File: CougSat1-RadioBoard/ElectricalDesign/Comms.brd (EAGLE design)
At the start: 91.4 x 95.8 mm, 427 parts, among them J1 230mm Antenna, J2 CougSat Card, J3 230mm Antenna, J4 SWD, Q1 CSD25402Q3A, Q10 DMN53D0LDW, Q11 MMBTA06W, Q12 MMBTA06W, Q13 DMN53D0LDW, Q14 DMP2065UFDB, Q15 MMBTA06W, Q16 CSD25402Q3A, Q17 CSD25402Q3A, Q2 CSD25402Q3A, Q3 CSD25402Q3A, Q4 DMN53D0LDW, Q5 DMN53D0LDW, Q6 CSD25402Q3A, Q7 CSD25402Q3A, Q8 CSD25402Q3A, Q9 DMN53D0LDW, U1 TPS73250, U10 MAAP-011232, U11 LTC2499, U12 LTC2499, U13 LTC2499, U14 LP5907MFX-3.1, U15 TPS73250, U16 AD8137, U17 STM32L496RGT, U18 AD8137, U19 MAAP-011232, U2 LP5907MFX-3.1, U20 ADF4360, U21 HMC545A, U22 AD8515, U23 MAAM-011229, U24 AD8515, U25 MAAM-011229, U26 AD8345, U27 LM2776, U28 AS8348, U29 MCP1501-18, U3 TPS61236, U30 TXS0102DQM, U31 MAAM-011229, U32 AD8515, U33 AD8515, U34 AD8515, U35 TXS0102DQM, U36 ADF4360, U37 AD8515, U38 AD8515, U39 AD8515, U4 AD8346, U40 AD8515, U41 AD8137, U42 AD8137, U43 LP5907MFX-3.1, U44 TPS73250, U5 ADF4360, U6 TPS61089, U7 MAAM-011229, U8 IS25LP016D, U9 IS25LP016D, Y1 20MHz ±2.5ppm, Y2 32.768kHz ±10ppm, Y3 16MHz ±10ppm, Y4 20MHz ±2.5ppm, Y5 20MHz ±2.5ppm

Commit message: Created mCAD
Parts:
- removed LOGO3: SIGNATUREBRADLEY, CougsInSpace-Aesthetics:SIGN-BRADLEY
- added LOGO201: Speed Limit, CougsInSpace-Aesthetics:SPEED_LIMIT
- LOGO1: value Speed Limit -> SIGNATUREBRADLEY; device CougsInSpace-Aesthetics:SPEED_LIMIT -> CougsInSpace-Aesthetics:SIGN-BRADLEY
- moved LOGO1 55.1 mm to (8.30, -2.70), flipped to the top
- renumbered C133 to C200, C134 to C201, C135 to C202, C136 to C203, C137 to C204, C138 to C205, C139 to C206, C140 to C207, C141 to C208, C142 to C209, C143 to C210, C144 to C211, C145 to C212, C146 to C213, C147 to C214, C148 to C215, C149 to C216, C150 to C217, C151 to C218, C152 to C219, C153 to C220, C154 to C221, C155 to C222, C156 to C223, C157 to C224, C158 to C225, C159 to C226, C160 to C227, C161 to C228, C162 to C229, C163 to C230, J4 to J200, LOGO2 to LOGO200, R125 to R200, R126 to R201, R127 to R202, R128 to R203, R129 to R204, R130 to R205, R131 to R206, RT10 to RT205, RT11 to RT206, RT12 to RT207, RT13 to RT208, RT14 to RT209, RT15 to RT210, RT16 to RT211, RT17 to RT212, RT18 to RT213, RT19 to RT214, RT20 to RT215, RT21 to RT216, RT22 to RT217, RT5 to RT200, RT6 to RT201, RT7 to RT202, RT8 to RT203, RT9 to RT204, TP1 to TP200, TP2 to TP201, TP3 to TP202, TP4 to TP203, TP5 to TP204, Z2 to Z1

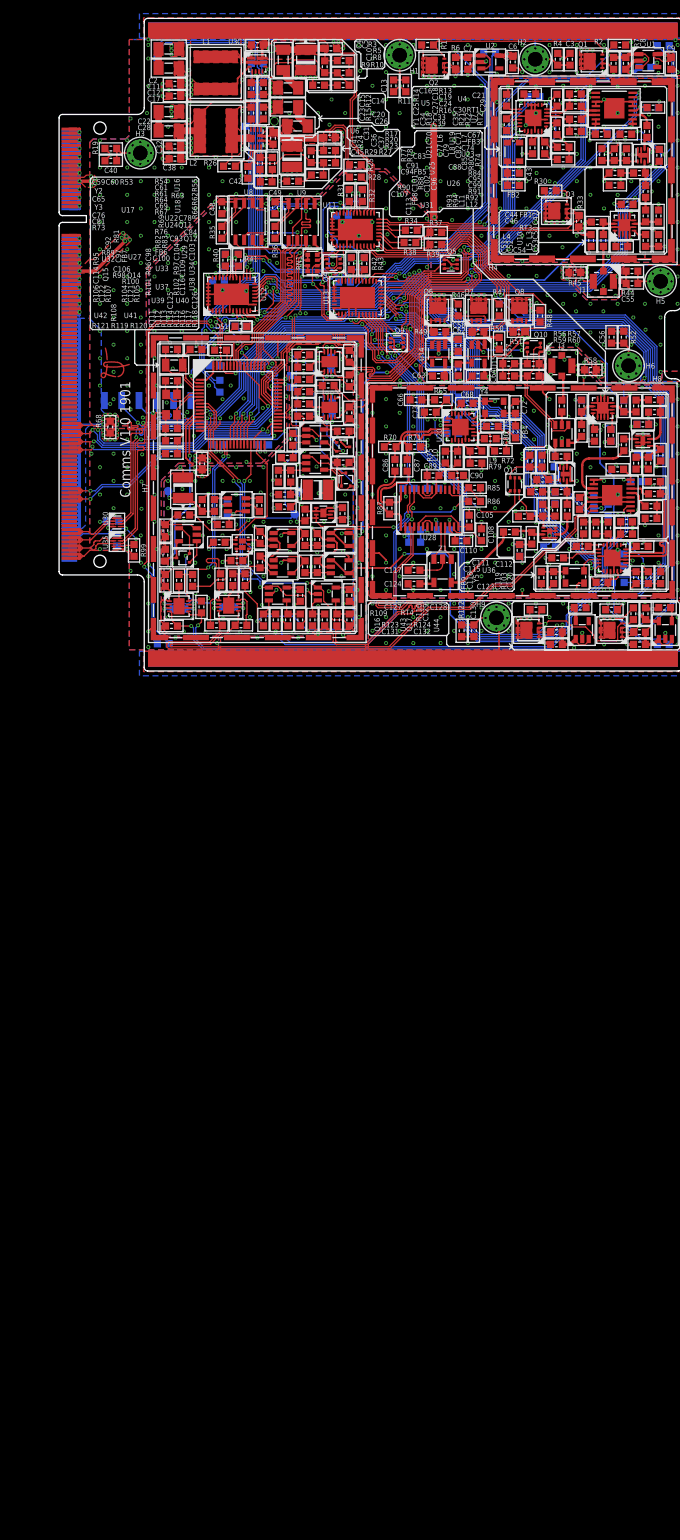
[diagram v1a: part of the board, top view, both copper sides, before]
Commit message: Edited ADCs and RF Clock Generators
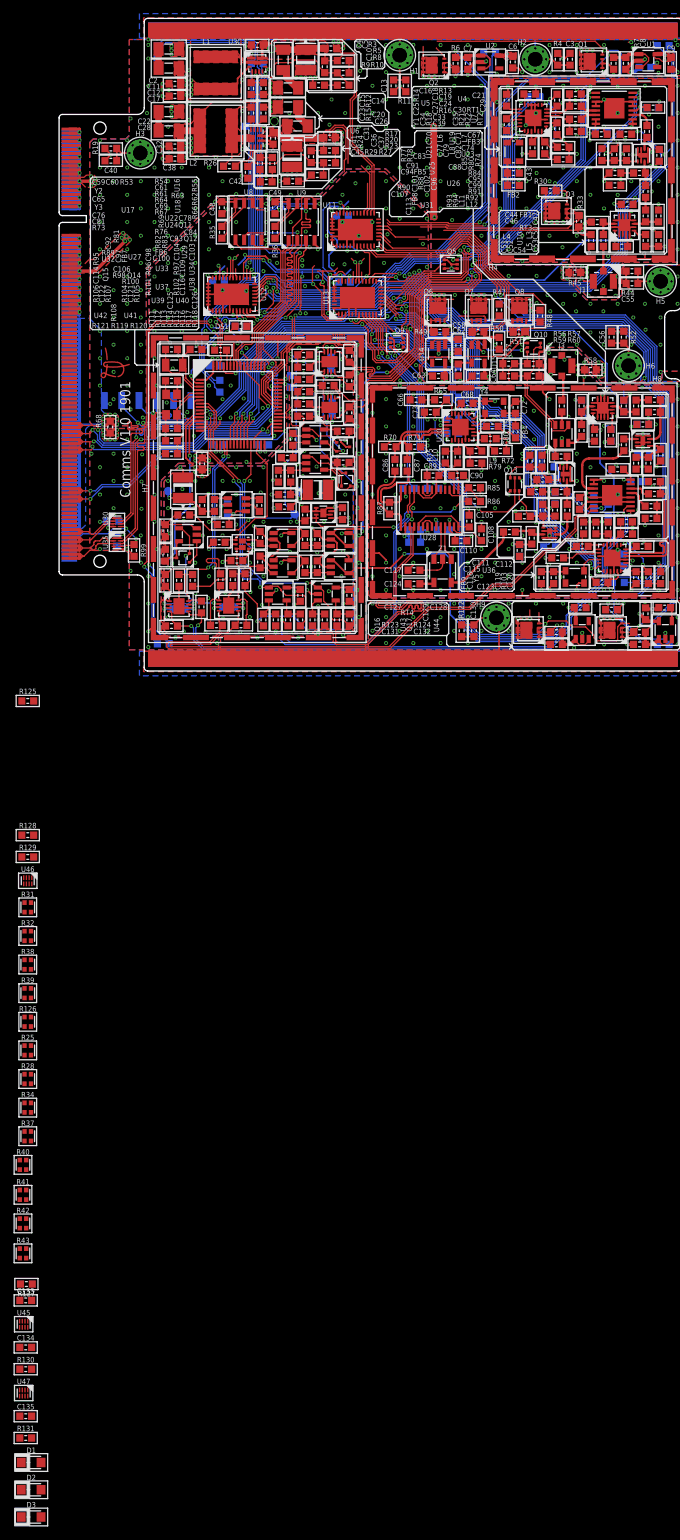
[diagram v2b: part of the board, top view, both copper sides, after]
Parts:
- removed Q4: DMN53D0LDW, CougsInSpace-DiscreteSemi:SOT363
- removed R1, R109, R110, R2, R46: 10kΩ 0.1%, CougsInSpace-Resistors:1608
- removed R201, R202, R203, R204, R205, R206: 8.45kΩ 0.1%, CougsInSpace-Resistors:1608
- removed RN1: 10kΩ 1%, CougsInSpace-Resistors:1632
- added C133, C134, C135: 100nF 10%, CougsInSpace-Capacitors:1608
- added D1, D2, D3: SS1FH10, CougsInSpace-DiscreteSemi:DO-219AB
- added R125: 1kΩ 0.1%, CougsInSpace-Resistors:1608
- added R126: 20kΩ 0.1%, CougsInSpace-Resistors:1616
- added R127, R128, R129, R130, R131: 10kΩ 0.1%, CougsInSpace-Resistors:1608
- added U45, U46, U47: TXS0102DQM, CougsInSpace-IC-Comms:X2SON-8
- R25, R37, R39: value 47kΩ 0.1% -> 50kΩ 0.1%; device CougsInSpace-Resistors:1608 -> CougsInSpace-Resistors:1616
- R28, R34, R38: value 47kΩ 0.1% -> 20kΩ 0.1%; device CougsInSpace-Resistors:1608 -> CougsInSpace-Resistors:1616
- R31, R40, R42: value 39.2kΩ 0.1% -> 20kΩ 0.1%; device CougsInSpace-Resistors:1608 -> CougsInSpace-Resistors:1616
- R32, R41, R43: value 39.2kΩ 0.1% -> 5kΩ 0.1%; device CougsInSpace-Resistors:1608 -> CougsInSpace-Resistors:1616
- moved R43 153.7 mm to (-5.30, -133.4), turned to 0 degrees
- moved R42 148.9 mm to (-5.30, -129.0), turned to 0 degrees
- moved R37 145.6 mm to (-4.60, -116.2), turned to 0 degrees
- moved R28 140.9 mm to (-4.60, -107.8)
- moved R41 140.8 mm to (-5.30, -124.8), turned to 0 degrees
- moved R34 140.6 mm to (-4.60, -112.0), turned to 0 degrees
- moved R25 138.6 mm to (-4.60, -103.6)
- moved R40 136.1 mm to (-5.30, -120.4), turned to 0 degrees
- moved R39 125.2 mm to (-4.60, -95.2), turned to 0 degrees
- moved R38 119.9 mm to (-4.60, -91.0), turned to 0 degrees
- moved R32 119.3 mm to (-4.60, -86.8), turned to 0 degrees
- moved R31 114.7 mm to (-4.60, -82.6), turned to 0 degrees
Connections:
- removed net I2C_SCL_5V: Q4.6, RN1.4, U11.2
- removed net I2C_SDA_5V: Q4.3, RN1.3, U11.3
- new net ADC_5.0V: R28.2, U11.20
- new net ADC_5.0V_I: R28.1, U11.21
- new net ADC_I_5.0V-0N: R34.1, U11.19
- new net ADC_I_5.0V-0P: R34.2, U11.18
- new net ADC_I_5.0V-1N: R126.4, U11.11
- new net ADC_I_5.0V-1P: R126.3, U11.10
- new net ADC_I_5.0V-2N: R38.4, U11.13
- new net ADC_I_5.0V-P: R38.3, U11.12
- new net PC_VHIGH: D1.C, D2.C, D3.C, R30.2, R47.2, R48.2
- new net RFCLK_MOSI-230: U46.6, U5.18
- new net RFCLK_MOSI-DEMOD: U20.18, U45.6
- new net RFCLK_MOSI-MOD: U36.18, U47.6
- new net RFCLK_SCK-230: U46.7, U5.17
- new net RFCLK_SCK-DEMOD: U20.17, U45.7
- new net RFCLK_SCK-MOD: U36.17, U47.7
- new net SWD_VSENSE: J200.1, R125.1
- net 3.3V: now also C133.1, C134.1, C135.1, C227.1, D1.A, R125.2, R128.2, R129.2, U11.28, U45.1, U45.8, U46.1, U46.8, U47.1, U47.8; no longer J200.1, Q4.2, Q4.5, R1.2, R109.2, R46.2, RN1.7, RN1.8
- net 3.3V_0: now also R127.2, U46.5
- net 3.3V_1: now also R131.2, U47.5
- net 3.3V_2: now also R130.2, U45.5
- net 5.0V: now also D2.A, R28.3; no longer C227.1, R110.2, R2.2, R47.2, RN1.5, RN1.6, U11.20, U11.28
- net 5.0V_I: now also R28.4; no longer U11.21
- net 9.0V: now also D3.A, R25.4; no longer R28.1, R30.2, R48.2
- net 9.0V_0: now also R37.3; no longer R37.1
- net 9.0V_1: now also R39.1; no longer R38.1
- net 9.0V_I: now also R25.3; no longer R25.1
- net ADC_9.0V: now also R25.1; no longer R28.2
- net ADC_9.0V_1: now also R39.4; no longer R38.2
- net ADC_ADCINN-0: now also R42.2, R43.3; no longer R204.2, R40.1
- net ADC_ADCINN-1: now also R31.2, R32.3; no longer R206.2, R31.1
- net ADC_ADCINN-2: now also R40.2, R41.3; no longer R202.2, R42.1
- net ADC_ADCINP-0: now also R42.1, R43.4; no longer R203.2, R41.1
- net ADC_ADCINP-1: now also R31.1, R32.4; no longer R205.2, R32.1
- net ADC_ADCINP-2: now also R40.1, R41.4; no longer R201.2, R43.1
- net ADC_I_9.0V_0: now also R37.1; no longer R34.2
- net ADC_I_9.0V_1: now also R39.3; no longer R39.2
- net ADC_MUXOUTN-0: now also R42.3; no longer R40.2
- net ADC_MUXOUTN-1: now also R31.3; no longer R31.2
- net ADC_MUXOUTN-2: now also R40.3; no longer R42.2
- net ADC_MUXOUTP-0: now also R42.4; no longer R41.2
- net ADC_MUXOUTP-1: now also R31.4; no longer R32.2
- net ADC_MUXOUTP-2: now also R40.4; no longer R43.2
- net AGND: now also R32.1, R32.2, R41.1, R41.2, R43.1, R43.2; no longer R201.1, R202.1, R203.1, R204.1, R205.1, R206.1
- net AVDD: no longer U11.29, U12.29, U13.29
- net AVREF: now also U11.29, U12.13, U12.29, U13.29; no longer U12.22
- net DGND: now also C133.2, C134.2, C135.2, R127.1, R130.1, R131.1, U11.9, U12.22, U45.4, U46.4, U47.4; no longer U12.13
- net I2C_SCL: now also R128.1, U11.2; no longer Q4.1, RN1.1
- net I2C_SDA: now also R129.1, U11.3; no longer Q4.4, RN1.2
- net I_5.0V-0N: now also R34.4; no longer U11.19
- net I_5.0V-0P: now also R34.3; no longer U11.18
- net I_5.0V-1N: now also R126.1; no longer U11.11
- net I_5.0V-1P: now also R126.2; no longer U11.10
- net I_5.0V-2N: now also R38.1; no longer U11.13
- net I_5.0V-2P: now also R38.2; no longer U11.12
- net I_9.0V_0: now also R37.4; no longer R34.1
- net I_9.0V_1: now also R39.2; no longer R39.1
- net PC_DEMOD: no longer R46.1
- net PC_MOD_230: no longer R1.1, R2.1
- net PC_MOD_700: no longer R109.1, R110.1
- net RFCLK_MOSI: now also U45.3, U46.3, U47.3; no longer U20.18, U36.18, U5.18
- net RFCLK_SCK: now also U45.2, U46.2, U47.2; no longer U20.17, U36.17, U5.17
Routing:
- net I2C_SCL_5V: track 7.68 -> 0.00 mm
- net 5.0V: track 235.9 -> 228.9 mm
- net I2C_SDA_5V: track 6.32 -> 0.00 mm, vias 2 -> 0
- net AGND: track 461.6 -> 455.4 mm
- net ADC_ADCINN-1: track 4.65 -> 0.00 mm, vias 1 -> 0
- net ADC_ADCINP-1: track 4.61 -> 0.00 mm, vias 1 -> 0
- net 3.3V: track 380.5 -> 376.2 mm
- net DGND: track 675.0 -> 671.7 mm
- net PC_MOD_230: track 84.0 -> 81.5 mm
- net RFCLK_SCK: track 145.6 -> 143.2 mm
- net I2C_SDA: track 43.6 -> 41.4 mm
- net ADC_9.0V_1: track 4.31 -> 2.29 mm
- net ADC_I_9.0V_0: track 4.18 -> 2.17 mm
- net ADC_MUXOUTP-1: track 1.95 -> 0.00 mm
- net ADC_MUXOUTN-1: track 1.91 -> 0.00 mm
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
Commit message: Wrote Testing 3.1
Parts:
- added C136, C137: 1nF 1%, CougsInSpace-Capacitors:1608
- added R1, R2, R46: 10kΩ 0.1%, CougsInSpace-Resistors:1608
- U28: value AS8348 -> AD8348
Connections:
- removed net PR_BATT-6: J2.77, J2.78, J2.79, J2.80
- new net DEMODE_MXI_P: C137.1, U28.18
- new net DEMOD_MXI_N: C136.1, U28.19
- new net PR_BATT-1: J2.57, J2.58, J2.59, J2.60
- net 3.3V: now also R1.2, R2.2, R46.2
- net PC_DEMOD_LV: now also R46.1
- net PC_MOD_230_LV: now also R1.1
- net PC_MOD_700_LV: now also R2.1
- net RFGND-1: now also C136.2, C137.2
- net VBATT: now also J2.77, J2.78, J2.79, J2.80; no longer J2.57, J2.58, J2.59, J2.60
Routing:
- net PR_BATT-6: track 7.20 -> 0.00 mm, vias 1 -> 0
- net VBATT: track 91.7 -> 85.7 mm

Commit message: Adjusted Layout After Part Changes
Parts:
- removed C200, C201, C202, C203, C204: 100nF 10%, CougsInSpace-Capacitors:1608
- removed Q17: CSD25402Q3A, CougsInSpace-DiscreteSemi:SON-3333
- removed R129, R130, R131: 10kΩ 0.1%, CougsInSpace-Resistors:1608
- removed R200: 1kΩ 0.1%, CougsInSpace-Resistors:1608
- removed U45, U46, U47: TXS0102DQM, CougsInSpace-IC-Comms:X2SON-8
- added C144, C145: 1nF 1%, CougsInSpace-Capacitors:1608
- added Q4: DMN53D0LDW, CougsInSpace-DiscreteSemi:SOT363
- added R109: 1.2kΩ 0.1%, CougsInSpace-Resistors:1608
- added R110: 10kΩ 0.1%, CougsInSpace-Resistors:1608
- C136, C137: value 1nF 1% -> 100nF 10%
- Q10: value DMN53D0LDW -> MMBTA06W; device CougsInSpace-DiscreteSemi:SOT363 -> CougsInSpace-DiscreteSemi:SOT323
- Q12: value MMBTA06W -> DMN53D0LDW; device CougsInSpace-DiscreteSemi:SOT323 -> CougsInSpace-DiscreteSemi:SOT363
- Q13: value DMN53D0LDW -> DMP2065UFDB; device CougsInSpace-DiscreteSemi:SOT363 -> CougsInSpace-DiscreteSemi:UDFN-6
- Q14: value DMP2065UFDB -> MMBTA06W; device CougsInSpace-DiscreteSemi:UDFN-6 -> CougsInSpace-DiscreteSemi:SOT323
- Q15: value MMBTA06W -> CSD25402Q3A; device CougsInSpace-DiscreteSemi:SOT323 -> CougsInSpace-DiscreteSemi:SON-3333
- Q5: value DMN53D0LDW -> CSD25402Q3A; device CougsInSpace-DiscreteSemi:SOT363 -> CougsInSpace-DiscreteSemi:SON-3333
- Q8: value CSD25402Q3A -> DMN53D0LDW; device CougsInSpace-DiscreteSemi:SON-3333 -> CougsInSpace-DiscreteSemi:SOT363
- R1, R47, R48: value 10kΩ 0.1% -> 50mΩ 1%
- R10: value 0Ω <20mΩ -> 102kΩ 0.1%
- R100: value 100kΩ 0.1% -> 1kΩ 0.1%
- R103: value 13.7kΩ 0.1% -> 100kΩ 0.1%
- R104, R64: value 3.3kΩ 0.1% -> 13.7kΩ 0.1%
- R108: value 1.2kΩ 0.1% -> 3.3kΩ 0.1%
- R11: value 0Ω <20mΩ -> 49.9Ω 0.1%
- R12: value 102kΩ 0.1% -> 4.7kΩ 0.1%
- R126: value 20kΩ 0.1% -> 5kΩ 0.1%
- R127, R128: value 10kΩ 0.1% -> 5kΩ 0.1%; device CougsInSpace-Resistors:1608 -> CougsInSpace-Resistors:1616
- R13: value 49.9Ω 0.1% -> 316kΩ 0.1%
- R14: value 4.7kΩ 0.1% -> 49.9Ω 0.1%
- R15: value 316kΩ 0.1% -> 50mΩ 1%
- R16: value 49.9Ω 0.1% -> 13.7kΩ 0.1%
- R17, R50, R51, R6: value 50mΩ 1% -> 0Ω <20mΩ
- R18: value 13.7kΩ 0.1% -> 30kΩ 1%
- R19, R53, R73: value 0Ω <20mΩ -> 2kΩ 0.1%
- R2: value 10kΩ 0.1% -> 0Ω <20mΩ
- R20: value 30kΩ 1% -> 2kΩ 0.1%
- R21: value 2kΩ 0.1% -> 0Ω <20mΩ
- R22: value 2kΩ 0.1% -> 10kΩ 0.1%
- R23: value 0Ω <20mΩ -> 442kΩ 1%
- R24, R35: value 10kΩ 0.1% -> 50kΩ 0.1%; device CougsInSpace-Resistors:1608 -> CougsInSpace-Resistors:1616
- R25: value 50kΩ 0.1% -> 0Ω <20mΩ; device CougsInSpace-Resistors:1616 -> CougsInSpace-Resistors:1608
- R26: value 442kΩ 1% -> 20kΩ 0.1%; device CougsInSpace-Resistors:1608 -> CougsInSpace-Resistors:1616
- R27: value 0Ω <20mΩ -> 4.7kΩ 0.1%
- R28, R34: value 20kΩ 0.1% -> 10kΩ 0.1%; device CougsInSpace-Resistors:1616 -> CougsInSpace-Resistors:1608
- R29: value 4.7kΩ 0.1% -> 20kΩ 0.1%; device CougsInSpace-Resistors:1608 -> CougsInSpace-Resistors:1616
- R3: value 50mΩ 1% -> 1MΩ 1%
- R30, R36: value 10kΩ 0.1% -> 20kΩ 0.1%; device CougsInSpace-Resistors:1608 -> CougsInSpace-Resistors:1616
- R31: value 20kΩ 0.1% -> 50mΩ 1%; device CougsInSpace-Resistors:1616 -> CougsInSpace-Resistors:1608
- R32: value 5kΩ 0.1% -> 50kΩ 0.1%
- R33: value 50mΩ 1% -> 10kΩ 0.1%
- R37: value 50kΩ 0.1% -> 10kΩ 0.1%; device CougsInSpace-Resistors:1616 -> CougsInSpace-Resistors:1608
- R39: value 50kΩ 0.1% -> 20kΩ 0.1%
- R4: value 0Ω <20mΩ -> 50mΩ 1%
- R41: value 5kΩ 0.1% -> 10kΩ 0.1%; device CougsInSpace-Resistors:1616 -> CougsInSpace-Resistors:1608
- R42: value 20kΩ 0.1% -> 0Ω <20mΩ; device CougsInSpace-Resistors:1616 -> CougsInSpace-Resistors:1608
- R43: value 5kΩ 0.1% -> 0Ω <20mΩ; device CougsInSpace-Resistors:1616 -> CougsInSpace-Resistors:1608
- R44, R45: value 0Ω <20mΩ -> 10kΩ 0.1%
- R5: value 1MΩ 1% -> 50mΩ 1%
- R52: value 0Ω <20mΩ -> 3.3kΩ 0.1%
- R54: value 3.3kΩ 0.1% -> 100kΩ 0.1%
- R55: value 2kΩ 0.1% -> 820kΩ 1%
- R56: value 100kΩ 0.1% -> 0Ω <20mΩ
- R57: value 820kΩ 1% -> 100kΩ 0.1%
- R58: value 0Ω <20mΩ -> 820kΩ 1%
- R59: value 100kΩ 0.1% -> 3.3kΩ 0.1%
- R60: value 820kΩ 1% -> 2kΩ 0.1%
- R61: value 3.3kΩ 0.1% -> 2kΩ 0.1%
- R62, R66: value 2kΩ 0.1% -> 3.3kΩ 0.1%
- R63: value 2kΩ 0.1% -> 1kΩ 0.1%
- R65: value 13.7kΩ 0.1% -> 2kΩ 0.1%
- R67: value 3.3kΩ 0.1% -> 0Ω <20mΩ
- R68: value 0Ω <20mΩ -> 200kΩ 0.1%
- R69: value 200kΩ 0.1% -> 49.9Ω 0.1%
- R7: value 50mΩ 1% -> 330kΩ 1%
- R71: value 49.9Ω 0.1% -> 4.7kΩ 0.1%
- R72: value 4.7kΩ 0.1% -> 0Ω <20mΩ
- R74: value 2kΩ 0.1% -> 470Ω 0.5%
- R75: value 470Ω 0.5% -> 100kΩ 0.1%
- R76: value 100kΩ 0.1% -> 10kΩ 0.1%
- R84: value 49.9Ω 0.1% -> 10kΩ 0.1%
- R85: value 20kΩ 0.5% -> 49.9Ω 0.1%
- R86: value 10kΩ 0.1% -> 20kΩ 0.5%
- R87: value 60.4Ω 0.1% -> 10kΩ 0.1%
- R88: value 2kΩ 0.1% -> 60.4Ω 0.1%
- R89: value 316kΩ 0.1% -> 2kΩ 0.1%
- R9: value 330kΩ 1% -> 0Ω <20mΩ
- R90: value 2kΩ 0.1% -> 316kΩ 0.1%
- R91: value 49.9Ω 0.1% -> 2kΩ 0.1%
- R92: value 470Ω 0.5% -> 49.9Ω 0.1%
- R93: value 4.7kΩ 0.1% -> 470Ω 0.5%
- R94: value 470Ω 0.5% -> 4.7kΩ 0.1%
- R95: value 200kΩ 0.1% -> 470Ω 0.5%
- R96: value 100kΩ 0.1% -> 200kΩ 0.1%
- R99: value 1kΩ 0.1% -> 100kΩ 0.1%
- moved R2 234.2 mm to (73.2, 41.9), turned to 270 degrees
- moved R1 223.7 mm to (39.9, 43.5)
- moved D3 193.8 mm to (74.0, 5.30)
- moved D2 193.1 mm to (72.5, 9.20), turned to 90 degrees
- moved R46 189.4 mm to (35.9, 2.90)
- moved D1 188.9 mm to (68.6, 10.3), turned to 180 degrees
- moved C136 171.1 mm to (67.6, -30.2), flipped to the bottom, turned to 270 degrees
- moved C137 169.3 mm to (52.2, -29.0), flipped to the bottom, turned to 180 degrees
- moved R42 165.9 mm to (84.1, 10.8)
- moved R43 165.2 mm to (75.7, 10.6), turned to 180 degrees
- moved C135 153.3 mm to (82.9, -31.6), flipped to the bottom, turned to 90 degrees
- moved R127 152.9 mm to (25.3, 12.0), flipped to the bottom
- moved R28 151.3 mm to (72.1, 22.6), turned to 180 degrees
- moved R41 142.8 mm to (37.7, 11.4), turned to 180 degrees
- moved R40 140.8 mm to (43.8, 11.6)
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- renumbered C205 to C138, C206 to C139, C207 to C140, C208 to C141, C209 to C142, C210 to C143, C211 to C146, C212 to C147, C213 to C148, C214 to C149, C215 to C150, C216 to C151, C217 to C152, C218 to C153, C219 to C154, C220 to C155, C221 to C156, C222 to C157, C223 to C158, C224 to C159, C225 to C160, C226 to C161, C227 to C162, C228 to C163, C229 to C164, C230 to C165, J200 to J4, LOGO200 to LOGO2, LOGO201 to LOGO3, RT200 to RT5, RT201 to RT6, RT202 to RT7, RT203 to RT8, RT204 to RT9, RT205 to RT10, RT206 to RT11, RT207 to RT12, RT208 to RT13, RT209 to RT14, RT210 to RT15, RT211 to RT16, RT212 to RT17, RT213 to RT18, RT214 to RT19, RT215 to RT20, RT216 to RT21, RT217 to RT22, TP200 to TP1, TP201 to TP2, TP202 to TP3, TP203 to TP4, TP204 to TP5
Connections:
- removed net RFCLK_MOSI-230: U46.6, U5.18
- removed net RFCLK_MOSI-DEMOD: U20.18, U45.6
- removed net RFCLK_MOSI-MOD: U36.18, U47.6
- removed net RFCLK_SCK-230: U46.7, U5.17
- removed net RFCLK_SCK-DEMOD: U20.17, U45.7
- removed net RFCLK_SCK-MOD: U36.17, U47.7
- new net PC_LDO_3.3V: Q15.4, Q2.4, Q5.4, R110.1, U17.39
- net !NRST: now also R72.1; no longer R73.1
- net !RX_LNA_EN: now also Q12.2, Q12.5; no longer Q13.2, Q13.5
- net 3.3V: now also D3.A, Q15.5, Q15.6, Q15.7, Q15.8, Q15.PAD, Q5.5, Q5.6, Q5.7, Q5.8, Q5.PAD, R110.2, R33.2, R34.2, R37.2, R41.2, R63.2, R76.2, R82.2; no longer C133.1, C134.1, C135.1, D1.A, Q16.5, Q16.6, Q16.7, Q16.8, Q16.PAD, Q6.5, Q6.6, Q6.7, Q6.8, Q6.PAD, R1.2, R125.2, R128.2, R129.2, R2.2, R35.2, R36.2, U45.1, U45.8, U46.1, U46.8, U47.1, U47.8
- net 3.3V_0: now also R11.2, R14.2; no longer R127.2, R13.2, R16.2, U46.5
- net 3.3V_1: now also C135.1, R85.2, R92.2; no longer C202.1, R131.2, R84.2, R91.2, U47.5
- net 3.3V_2: now also R69.2; no longer R130.2, R71.2, U45.5
- net 5.0V: now also D1.A, Q16.5, Q16.6, Q16.7, Q16.8, Q16.PAD, Q6.5, Q6.6, Q6.7, Q6.8, Q6.PAD, R1.2, R26.3; no longer D2.A, Q17.5, Q17.6, Q17.7, Q17.8, Q17.PAD, Q7.5, Q7.6, Q7.7, Q7.8, Q7.PAD, R28.3, R3.2
- net 5.0V_0: now also R20.2; no longer R22.2
- net 5.0V_1: now also R73.2; no longer R74.2
- net 5.0V_2: now also C136.1, C137.1, R91.2; no longer C203.1, C204.1, R90.2
- net 5.0V_I: now also R1.1, R26.4, R3.2; no longer R28.4, R3.1, R5.2
- net 9.0V: now also D2.A, Q7.5, Q7.6, Q7.7, Q7.8, Q7.PAD, R15.2, R24.4; no longer D3.A, Q8.5, Q8.6, Q8.7, Q8.8, Q8.PAD, R17.2, R25.4
- net 9.0V_0: now also R31.2, R32.3; no longer R33.2, R37.3
- net 9.0V_1: now also R35.4, R49.2, R54.2, R57.2; no longer R39.1, R51.2, R56.2, R59.2
- net 9.0V_I: now also R15.1, R18.2, R24.3; no longer R17.1, R20.2, R25.3
- net ADC_5.0V: now also R26.2; no longer R28.2
- net ADC_5.0V_I: now also R26.1; no longer R28.1
- net ADC_9.0V: now also R24.1; no longer R25.1
- net ADC_9.0V_0: now also R32.2; no longer R37.2
- net ADC_9.0V_1: now also R35.1; no longer R39.4
- net ADC_9.0V_I: now also R24.2; no longer R25.2
- net ADC_ADCINN-0: now also R127.4, R38.1; no longer R42.2, R43.3
- net ADC_ADCINN-1: now also R128.4, R29.1; no longer R31.2, R32.3
- net ADC_ADCINN-2: now also R126.4, R40.1; no longer R40.2, R41.3
- net ADC_ADCINP-0: now also R127.3, R38.2; no longer R42.1, R43.4
- net ADC_ADCINP-1: now also R128.3, R29.2; no longer R31.1, R32.4
- net ADC_ADCINP-2: now also R126.3, R40.2; no longer R40.1, R41.4
- net ADC_I_5.0V-0N: now also R30.1; no longer R34.1
- net ADC_I_5.0V-0P: now also R30.2; no longer R34.2
- net ADC_I_5.0V-1N: now also R39.1; no longer R126.4
- net ADC_I_5.0V-1P: now also R39.2; no longer R126.3
- net ADC_I_5.0V-2N: now also R36.1; no longer R38.4
- net ADC_I_5.0V-P: now also R36.2; no longer R38.3
- net ADC_I_9.0V_0: now also R32.1; no longer R37.1
- net ADC_I_9.0V_1: now also R35.2; no longer R39.3
- net ADC_MUXOUTN-0: now also R38.4; no longer R42.3
- net ADC_MUXOUTN-1: now also R29.4; no longer R31.3
- net ADC_MUXOUTN-2: now also R40.4; no longer R40.3
- net ADC_MUXOUTP-0: now also R38.3; no longer R42.4
- net ADC_MUXOUTP-1: now also R29.3; no longer R31.4
- net ADC_MUXOUTP-2: now also R40.3; no longer R40.4
- net AGND: now also Q13.2, Q13.5, R101.1, R126.1, R126.2, R127.1, R127.2, R128.1, R128.2, R68.1, R83.1, R96.1, R99.1; no longer Q14.2, Q14.5, R100.1, R32.1, R32.2, R41.1, R41.2, R43.1, R43.2, R69.1, R82.1, R95.1, R98.1
- net AMP_230_I_IN+: now also R61.1, R62.2; no longer R63.1, R64.2
- net AMP_230_I_IN-: now also R65.1, R66.2; no longer R66.1, R67.2
- net AMP_230_Q_IN+: now also R52.2, R53.1; no longer R54.2, R55.1
- net AMP_230_Q_IN-: now also R59.2, R60.1; no longer R61.2, R62.1
- net AMP_700_I_IN+: now also R108.2, R109.1; no longer R107.2, R108.1
- net AMP_700_I_IN-: now also R107.2; no longer R106.2
- net AMP_700_Q_IN+: now also R106.2; no longer R105.2
- net AMP_700_Q_IN-: now also R105.2; no longer R104.2
- net ANTENNA_SW: now also Q9.2; no longer Q10.2
- net ANTENNA_SW_A: now also Q9.5, Q9.6, R57.1, R58.2; no longer Q10.5, Q10.6, R59.1, R60.2
- net ANTENNA_SW_B: now also Q9.3, R54.1, R55.2; no longer Q10.3, R56.1, R57.2
- net AVDD: now also C133.1, C134.1, Q10.3, Q14.3, R84.2; no longer C200.1, C201.1, Q12.3, Q15.3, R83.2
- net AVDD_NEG: now also C133.2, C134.2, R102.1, R97.1; no longer C200.2, C201.2, R101.1, R96.1
- net AVREF: now also R75.2, R87.2, R90.2, U12.22; no longer R76.2, R86.2, R89.2, U12.13
- net BOOT0: now also R51.2; no longer R53.2
- net CHASSIS: now also R17.2, R2.2, R42.2, R50.2, R9.2; no longer R11.2, R19.2, R4.2, R44.2, R52.2
- net CTRL_!RESET: now also R72.2; no longer R73.2
- net DEMODE_MXI_P: now also C144.1; no longer C137.1
- net DEMOD_700_LOI_N: now also R88.1; no longer R87.1
- net DEMOD_700_LOI_P: now also R88.2; no longer R87.2
- net DEMOD_MXI_N: now also C145.1; no longer C136.1
- net DEMOD_VGIN: now also R86.2, R87.1; no longer R85.2, R86.1
- net DGND: now also R100.1, R125.1, R51.1, R67.1, U12.13; no longer C133.2, C134.2, C135.2, R127.1, R130.1, R131.1, R200.1, R53.1, R68.1, R99.1, U12.22, U45.4, U46.4, U47.4
- net FLASH_HOLD-A: now also R33.1; no longer R35.1
- net FLASH_HOLD-B: now also R34.1; no longer R36.1
- net I2C_SCL: now also R37.1; no longer R128.1
- net I2C_SDA: now also R41.1; no longer R129.1
- net I_3.3V-0N: now also R4.1; no longer R6.1
- net I_3.3V-0P: now also R4.2; no longer R6.2
- net I_3.3V-1P: now also Q15.1, Q15.2, Q15.3; no longer Q16.1, Q16.2, Q16.3
- net I_3.3V-2N: now also R47.1; no longer R49.1
- net I_3.3V-2P: now also Q5.1, Q5.2, Q5.3, R47.2; no longer Q6.1, Q6.2, Q6.3, R49.2
- net I_5.0V-0N: now also R30.4, R5.1; no longer R34.4, R7.1
- net I_5.0V-0P: now also R30.3, R5.2; no longer R34.3, R7.2
- net I_5.0V-1N: now also R39.4; no longer R126.1
- net I_5.0V-1P: now also Q16.1, Q16.2, Q16.3, R39.3; no longer Q17.1, Q17.2, Q17.3, R126.2
- net I_5.0V-2N: now also R36.4, R48.1; no longer R38.1, R50.1
- net I_5.0V-2P: now also Q6.1, Q6.2, Q6.3, R36.3, R48.2; no longer Q7.1, Q7.2, Q7.3, R38.2, R50.2
- net I_9.0V_0: now also R31.1, R32.4; no longer R33.1, R37.4
- net I_9.0V_1: now also Q7.1, Q7.2, Q7.3, R35.3, R49.1; no longer Q8.1, Q8.2, Q8.3, R39.2, R51.1
- net JTAG_EN_COMMS: now also R100.2; no longer R99.2
- net LED_C: now also R125.2; no longer R200.2
- net MOD_230_ID: now also R66.1; no longer R67.1
- net MOD_230_ID_N: now also R61.2; no longer R63.2
- net MOD_230_ID_P: now also R65.2; no longer R66.2
- net MOD_230_QD: now also R59.1; no longer R61.1
- net MOD_230_QD_N: now also R53.2; no longer R55.2
- net MOD_230_QD_P: now also R60.2; no longer R62.2
- net MOD_700_ID: now also R107.1; no longer R106.1
- net MOD_700_ID_N: now also R109.2; no longer R108.2
- net MOD_700_QD: now also R105.1; no longer R104.1
- net PA_230_BIAS: now also Q13.4, R99.2; no longer Q14.4, R98.2
- net PA_230_BIAS_AMPIN-0: now also Q13.3, Q13.PAD-BTM, R97.2; no longer Q14.3, Q14.PAD-BTM, R96.2
- net PA_230_BIAS_AMPIN-1: now also R98.2; no longer R97.2
- net PA_230_BIAS_AMPOUT-0: now also R98.1; no longer R97.1
- net PA_700_BIAS: now also Q13.1, R101.2; no longer Q14.1, R100.2
- net PA_700_BIAS_AMPIN-0: now also Q13.6, Q13.PAD-TOP, R102.2; no longer Q14.6, Q14.PAD-TOP, R101.2
- net PA_700_BIAS_AMPIN-1: now also R103.2; no longer R102.2
- net PA_700_BIAS_AMPOUT-0: now also R103.1; no longer R102.1
- net PC_DEMOD: now also Q8.3, R44.1; no longer Q7.4, Q9.3, R47.1
- net PC_DEMOD_LV: now also Q8.5, R82.1; no longer Q9.5, R46.1
- net PC_MOD_230: now also Q4.6, R28.1; no longer Q2.4, Q5.6, R30.1
- net PC_MOD_230_LV: now also Q4.2, R46.1; no longer Q5.2, R1.1
- net PC_MOD_700: now also Q7.4, Q8.6, R45.1; no longer Q17.4, Q8.4, Q9.6, R48.1
- net PC_MOD_700_LV: now also Q8.2, R76.1; no longer Q9.2, R2.1
- net PC_VHIGH: now also R28.2, R44.2, R45.2; no longer R30.2, R47.2, R48.2
- net PGND: now also Q4.1, Q4.3, Q4.4, Q4.5, Q8.1, Q8.4, R10.1, R13.1, R17.1, R2.1, R27.1, R42.1, R43.2, R50.1, R55.1, R56.2, R58.1, R67.2, R7.1; no longer Q10.1, Q10.4, Q5.1, Q5.3, Q5.4, Q5.5, R11.1, R12.1, R15.1, R19.1, R29.1, R4.1, R44.1, R45.2, R52.1, R57.1, R58.2, R60.1, R68.2
- net PREAMP_230_BIAS: now also R19.2, R20.1; no longer R21.2, R22.1
- net PREAMP_700_BIAS: now also R73.1; no longer R74.1
- net REG_CC-5: now also R10.2; no longer R12.2
- net REG_COMP-9: now also R22.2; no longer R24.2
- net REG_COMP_RC-9: now also R22.1; no longer R24.1
- net REG_FB-5: now also R6.1, R8.2; no longer R10.2, R8.1
- net REG_FB-9: now also R21.1, R25.2; no longer R23.1, R27.2
- net REG_FB_RES-HIGH-5: now also R3.1, R6.2; no longer R5.1, R8.2
- net REG_FB_RES-HIGH-9: now also R18.1, R21.2; no longer R20.1, R23.2
- net REG_FB_RES-LOW-5: now also R7.2, R8.1; no longer R10.1, R9.2
- net REG_FB_RES-LOW-9: now also R25.1, R27.2; no longer R27.1, R29.2
- net REG_FSW-9: now also R23.1; no longer R26.1
- net REG_ILIM-9: now also R13.2; no longer R15.2
- net REG_SW-9: now also R23.2; no longer R26.2
- net RFCLK_CP-230: now also R16.2; no longer R18.2
- net RFCLK_CP-DEMOD: now also R64.2; no longer R65.2
- net RFCLK_CP-MOD: now also R104.2; no longer R103.2
- net RFCLK_L1-DEMOD: now also R74.2; no longer R75.2
- net RFCLK_L1-MOD: now also R93.2; no longer R92.2
- net RFCLK_L2-MOD: now also R95.2; no longer R94.2
- net RFCLK_MOSI: now also U20.18, U36.18, U5.18; no longer U45.3, U46.3, U47.3
- net RFCLK_OUT-230_N: now also R11.1; no longer R13.1
- net RFCLK_OUT-230_P: now also R14.1; no longer R16.1
- net RFCLK_OUT-DEMOD_N: now also R70.1; no longer R71.1
- net RFCLK_OUT-DEMOD_P: now also R69.1; no longer R70.1
- net RFCLK_OUT-MOD_N: now also R92.1; no longer R91.1
- net RFCLK_OUT-MOD_P: now also R85.1; no longer R84.1
- net RFCLK_RSET-230: now also R12.2; no longer R14.2
- net RFCLK_RSET-DEMOD: now also R71.2; no longer R72.2
- net RFCLK_RSET-MOD: now also R94.2; no longer R93.2
- net RFCLK_SCK: now also U20.17, U36.17, U5.17; no longer U45.2, U46.2, U47.2
- net RFCLK_VTUNE_FILTER-230: now also R16.1; no longer R18.1
- net RFCLK_VTUNE_FILTER-DEMOD: now also R64.1; no longer R65.1
- net RFCLK_VTUNE_FILTER-MOD: now also R104.1; no longer R103.1
- net RFGND-0: now also R12.1, R19.1, R43.1; no longer R14.1, R21.1, R45.1
- net RFGND-1: now also C135.2, C144.2, C145.2, Q12.1, Q12.4, R56.1, R71.1, R74.1, R86.1, R89.1, R95.1; no longer C202.2, C203.2, C204.2, Q13.1, Q13.4, R58.1, R72.1, R75.1, R85.1, R88.1, R92.1
- net RX_LNA_BIAS-0: now also Q12.6; no longer Q13.6
- net RX_LNA_BIAS-1: now also Q12.3, R89.2, R91.1; no longer Q13.3, R88.2, R90.1
- net SWD_VSENSE: now also R63.1; no longer R125.1
- net VREF_CM_IN: now also Q11.2, R106.1, R108.1, R52.1, R62.1; no longer Q12.2, R105.1, R107.1, R54.1, R64.1
- net VREF_CM_IN_AMP_IN: now also R83.2, R84.1; no longer R82.2, R83.1
- net VREF_CM_IN_AMP_OUT: now also Q11.1; no longer Q12.1
- net VREF_CM_OUT_230: now also Q10.2; no longer Q11.2
- net VREF_CM_OUT_700: now also Q14.2; no longer Q15.2
- net VREF_CM_OUT_AMP_IN_230: now also R68.2, R75.1; no longer R69.2, R76.1
- net VREF_CM_OUT_AMP_IN_700: now also R90.1, R96.2; no longer R89.1, R95.2
- net VREF_CM_OUT_AMP_OUT_230: now also Q10.1; no longer Q11.1
- net VREF_CM_OUT_AMP_OUT_700: now also Q14.1; no longer Q15.1
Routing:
- net PC_LDO_3.3V: track 0.00 -> 176.6 mm, vias 0 -> 7
- net 3.3V: track 376.2 -> 423.5 mm, vias 33 -> 34
- net PC_VHIGH: track 0.00 -> 34.8 mm, vias 0 -> 4
- net PC_MOD_230: track 81.5 -> 53.7 mm
- net AVREF: track 114.8 -> 141.8 mm, vias 10 -> 12
- net 5.0V: track 228.9 -> 205.1 mm, vias 16 -> 14
- net AVDD: track 768.4 -> 744.9 mm, vias 38 -> 36
- net VBATT: track 85.7 -> 98.4 mm
- net I_5.0V-2N: track 39.9 -> 32.2 mm
- net I_5.0V-2P: track 37.1 -> 29.8 mm
- net PR_BATT-1: track 0.00 -> 7.20 mm, vias 0 -> 1
- net ADC_I_5.0V-P: track 0.00 -> 6.92 mm
- net I2C_SDA: track 41.4 -> 47.9 mm
- net ADC_I_5.0V-2N: track 0.00 -> 6.47 mm
- net I_9.0V_1: track 24.3 -> 30.3 mm
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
